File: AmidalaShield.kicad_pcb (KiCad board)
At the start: 4 copper layers, 106 x 73 mm, 32 parts, among them J1 Screw_Terminal_01x02, J2 Micro_SD_Card

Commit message: Switched SD Card slots
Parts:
- removed J2: Micro_SD_Card, Connector_Card:microSD_HC_Wuerth_693072010801
- added J3: Micro_SD_Card, Connector_Card:microSD_HC_Hirose_DM3AT-SF-PEJM5, F.Cu at (146.6, 48.7)
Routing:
- net GND: track 61.9 -> 73.6 mm
- net /SPI/GPIO11: track 133.9 -> 123.2 mm
- net +3.3V: track 106.5 -> 98.7 mm
- net /SPI/GPIO12: track 179.4 -> 171.9 mm
- net /SPI/GPIO13: track 178.9 -> 172.4 mm
- net /SPI/GPIO10: track 86.9 -> 83.8 mm

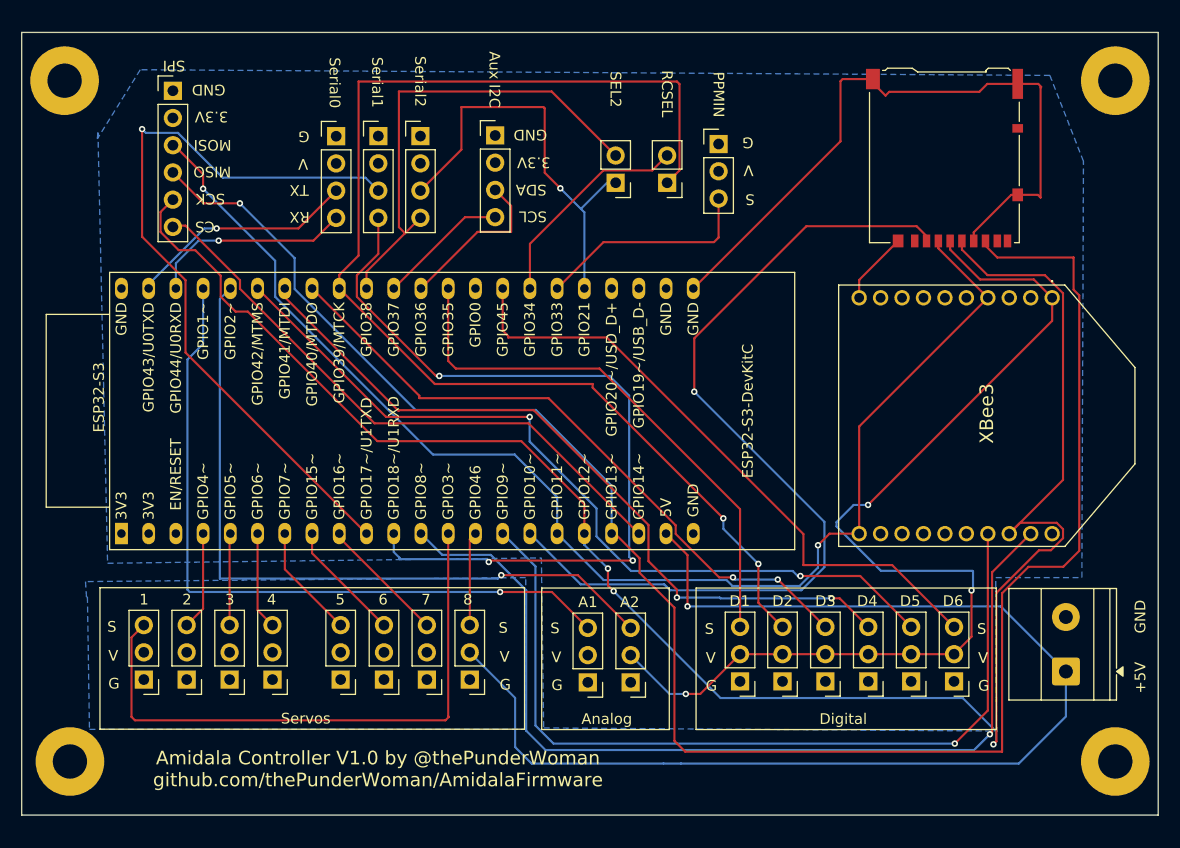
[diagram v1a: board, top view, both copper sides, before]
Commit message: Remapped GPIOs for clean routing
This updates the GPIO table so that the traces and vias are far cleaner. Slight repositioning of some pins to account for that. Rebuilt all gerbers and necessary stuff.
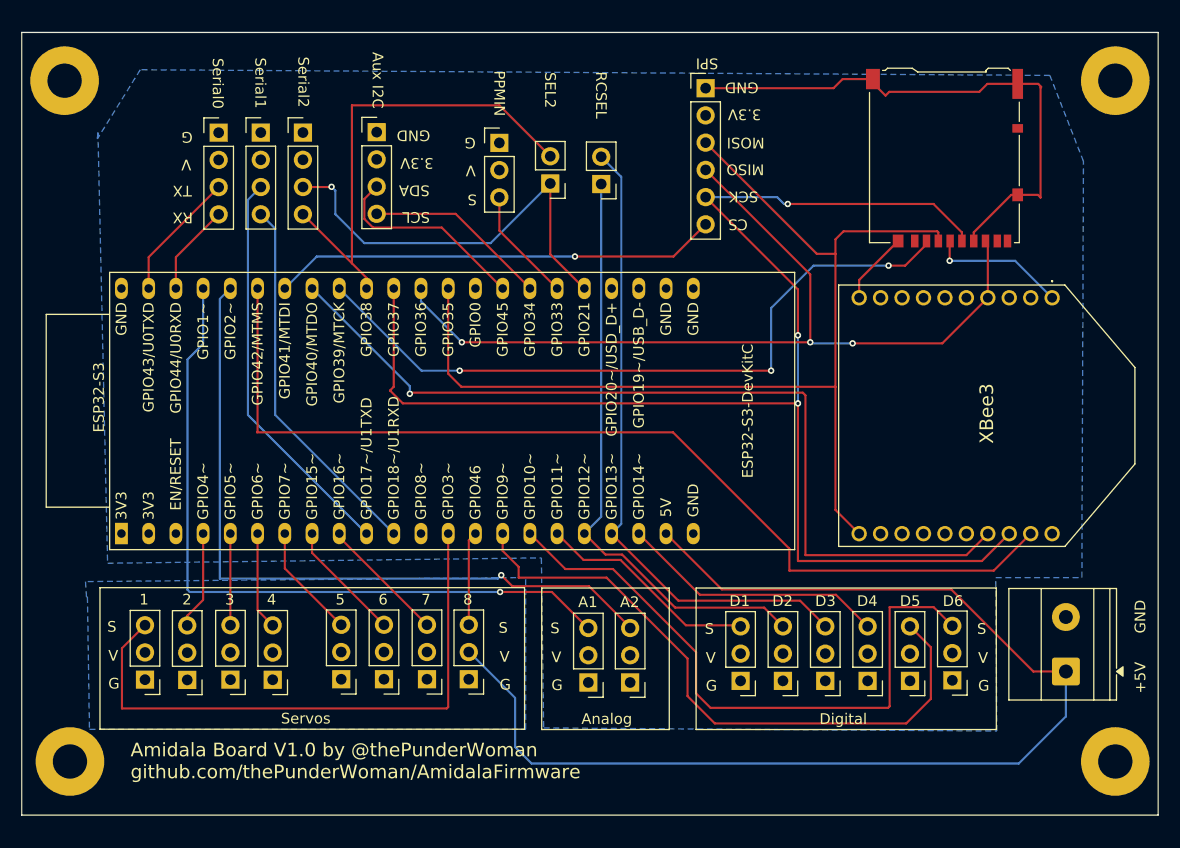
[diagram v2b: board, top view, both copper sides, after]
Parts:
- moved SPI1 49.7 mm to (124.3, 42.2)
- moved J_PPMIN1 20.5 mm to (105.0, 47.3)
- moved I2C1 11.1 mm to (93.6, 46.3)
- moved Serial1 11.0 mm to (82.8, 46.3)
- moved SWSerial1 11.0 mm to (86.7, 46.3)
- moved Serial0 11.0 mm to (78.9, 46.4)
- moved J_RCSEL1 6.15 mm to (114.5, 51.1)
- moved J_SEL2 6.10 mm to (109.8, 51.1)
- moved J_Digital6 0.19 mm to (147.3, 97.4)
- moved J_Digital5 0.12 mm to (143.3, 97.5)
- moved J_Servo1 0.11 mm to (72.0, 97.4)
- moved J_Servo8 0.09 mm to (102.2, 97.3)
- moved J_Servo3 0.08 mm to (80.0, 97.4)
- moved J_Digital4 0.08 mm to (139.4, 97.5)
- moved J_Digital1 0.07 mm to (127.5, 97.5)
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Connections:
- ESP32-S3 pad 12: /SPI/GPIO8 -> unconnected-(ESP32-S3-GPIO8/ADC1_CH7-Pad12)
- ESP32-S3 pad 15: /SPI/GPIO9 -> /Pins/GPIO9
- ESP32-S3 pad 16: /SPI/GPIO10 -> /Pins/GPIO10
- ESP32-S3 pad 17: /SPI/GPIO11 -> /Pins/GPIO11
- ESP32-S3 pad 18: /SPI/GPIO12 -> /Pins/GPIO12
- ESP32-S3 pad 19: /SPI/GPIO13 -> /Pins/GPIO13
- ESP32-S3 pad 20: /SPI/GPIO14 -> /Pins/GPIO14
- ESP32-S3 pad 29: /RC Control/GPIO48 -> /Comms/GPIO48
- ESP32-S3 pad 30: /Pins/GPIO45 -> /Comms/GPIO45
- ESP32-S3 pad 32: /Pins/GPIO35 -> /SPI/GPIO35
- ESP32-S3 pad 33: /Comms/GPIO36 -> /SPI/GPIO36
- ESP32-S3 pad 34: /Comms/GPIO37 -> /SPI/GPIO37
- ESP32-S3 pad 36: /Pins/GPIO39 -> /SPI/GPIO39
- ESP32-S3 pad 37: /Pins/GPIO40 -> /SPI/GPIO40
- ESP32-S3 pad 38: /Pins/GPIO41 -> /SPI/GPIO41
- ESP32-S3 pad 39: /Pins/GPIO42 -> /SPI/GPIO42
- I2C1 pad 3: /Comms/GPIO36 -> /Comms/GPIO45
- I2C1 pad 4: /Comms/GPIO37 -> /Comms/GPIO48
- J3 pad 2: /SPI/GPIO10 -> /SPI/GPIO39
- J3 pad 3: /SPI/GPIO11 -> /SPI/GPIO35
- J3 pad 5: /SPI/GPIO12 -> /SPI/GPIO37
- J3 pad 7: /SPI/GPIO13 -> /SPI/GPIO36
- J_Digital1 pad 3: /Pins/GPIO35 -> /Pins/GPIO11
- J_Digital2 pad 3: /Pins/GPIO39 -> /Pins/GPIO12
- J_Digital3 pad 3: /Pins/GPIO40 -> /Pins/GPIO13
- J_Digital4 pad 3: /Pins/GPIO41 -> /Pins/GPIO14
- J_Digital5 pad 3: /Pins/GPIO42 -> /Pins/GPIO9
- J_Digital6 pad 3: /Pins/GPIO45 -> /Pins/GPIO10
- J_RCSEL1 pad 1: /Pins/GPIO39 -> /Pins/GPIO12
- J_RCSEL1 pad 2: /RC Control/GPIO48 -> /Pins/GPIO13
- SPI1 pad 3: /SPI/GPIO11 -> /SPI/GPIO35
- SPI1 pad 4: /SPI/GPIO13 -> /SPI/GPIO36
- SPI1 pad 5: /SPI/GPIO12 -> /SPI/GPIO37
- SPI1 pad 6: /SPI/GPIO14 -> /SPI/GPIO41
- XBee3 pad 11: /SPI/GPIO11 -> /SPI/GPIO35
- XBee3 pad 17: /SPI/GPIO9 -> /SPI/GPIO40
- XBee3 pad 18: /SPI/GPIO12 -> /SPI/GPIO37
- XBee3 pad 19: /SPI/GPIO8 -> /SPI/GPIO42
- XBee3 pad 4: /SPI/GPIO11 -> /SPI/GPIO36
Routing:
- net /SPI/GPIO13: track 172.4 -> 0.00 mm, vias 1 -> 0
- net /SPI/GPIO12: track 171.9 -> 0.00 mm, vias 3 -> 0
- net /SPI/GPIO37: track 0.00 -> 132.6 mm, vias 0 -> 3
- net /SPI/GPIO11: track 123.2 -> 0.00 mm, vias 2 -> 0
- net /Pins/GPIO39: track 117.1 -> 0.00 mm, vias 2 -> 0
- net /SPI/GPIO35: track 0.00 -> 100.1 mm
- net /SPI/GPIO42: track 0.00 -> 93.6 mm
- net /SPI/GPIO8: track 90.0 -> 0.00 mm, vias 1 -> 0
- net +3.3V: track 98.7 -> 12.9 mm, vias 3 -> 1
- net /SPI/GPIO10: track 83.8 -> 0.00 mm, vias 1 -> 0
- net /SPI/GPIO40: track 0.00 -> 83.4 mm, vias 0 -> 1
- net /SPI/GPIO36: track 0.00 -> 83.0 mm, vias 0 -> 3
- net /SPI/GPIO9: track 79.8 -> 0.00 mm, vias 1 -> 0
- net /Pins/GPIO42: track 76.9 -> 0.00 mm, vias 2 -> 0
- net /Pins/GPIO41: track 70.4 -> 0.00 mm, vias 2 -> 0
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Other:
- board text added: "Amidala Board V1.0 by @thePunderWoman github.com/thePunderWoman/AmidalaFirmware"
- board text removed: "Amidala Controller V1.0 by @thePunderWoman github.com/thePunderWoman/AmidalaFirmware"

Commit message: final pass safety check
This verified that the XBee had all the pins wired up correctly with the proper resistor and cap connections. Glad I caught this before getting them fabbed.
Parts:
- added C1: 100n, Capacitor_SMD:C_0603_1608Metric, F.Cu at (134.1, 60.7)
- added R1: 10k, Resistor_SMD:R_0603_1608Metric, F.Cu at (161.6, 55.2)
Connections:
- ESP32-S3 pad 12: unconnected-(ESP32-S3-GPIO8/ADC1_CH7-Pad12) -> /SPI/GPIO8
- XBee3 pad 13: unconnected-(XBee3-ON/~{SLEEP}/DIO9-Pad13) -> /SPI/GPIO8
- XBee3 pad 5: unconnected-(XBee3-~{RESET}-Pad5) -> Net-(XBee3-~{RESET})
- XBee3 pad 9: unconnected-(XBee3-~{DTR}/SLEEP_RQ/DIO8-Pad9) -> GND
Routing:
- net /SPI/GPIO8: track 0.00 -> 47.7 mm, vias 0 -> 1
- net Net-(XBee3-~{RESET}): track 0.00 -> 32.6 mm, vias 0 -> 2
- net +3.3V: track 12.9 -> 21.8 mm
- net GND: track 61.0 -> 66.5 mm, vias 0 -> 1
- net /SPI/GPIO36: track 83.0 -> 85.3 mm

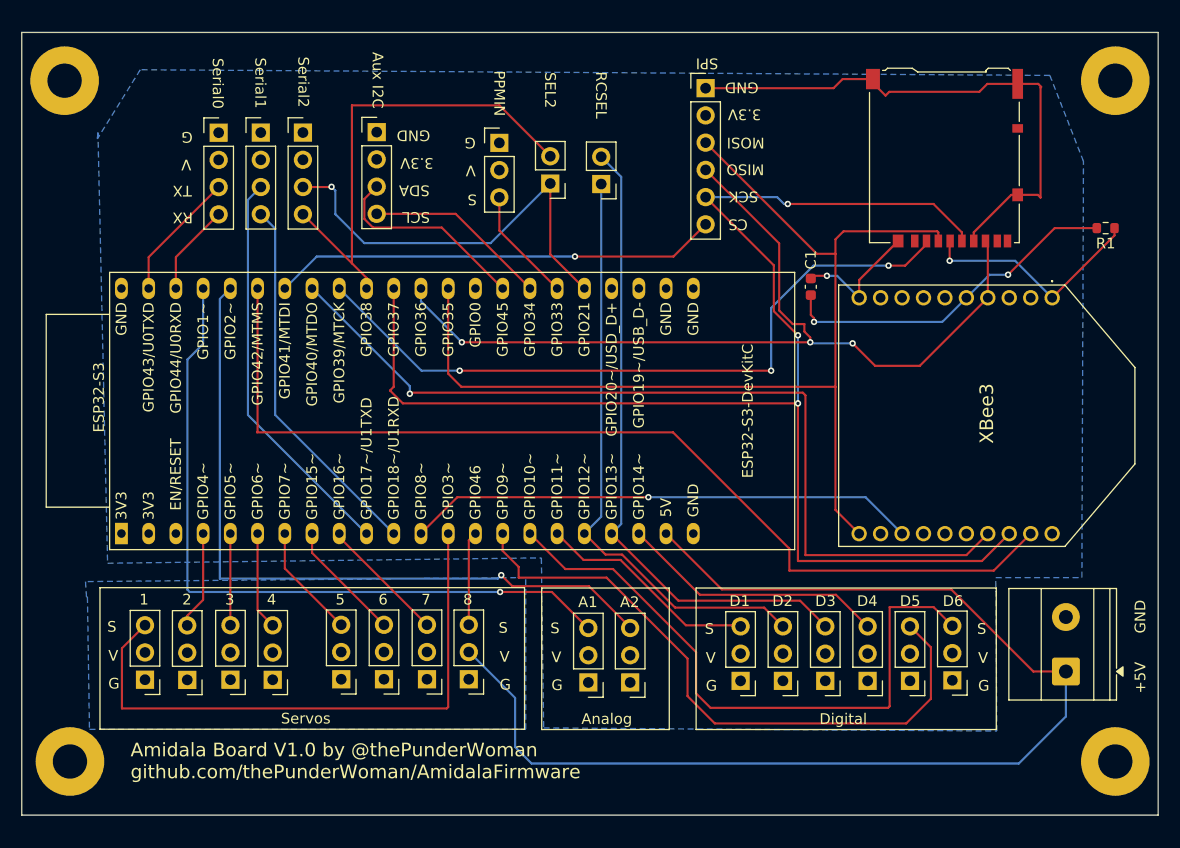
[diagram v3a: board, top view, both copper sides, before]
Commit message: Updated to v1.1 to fix issues
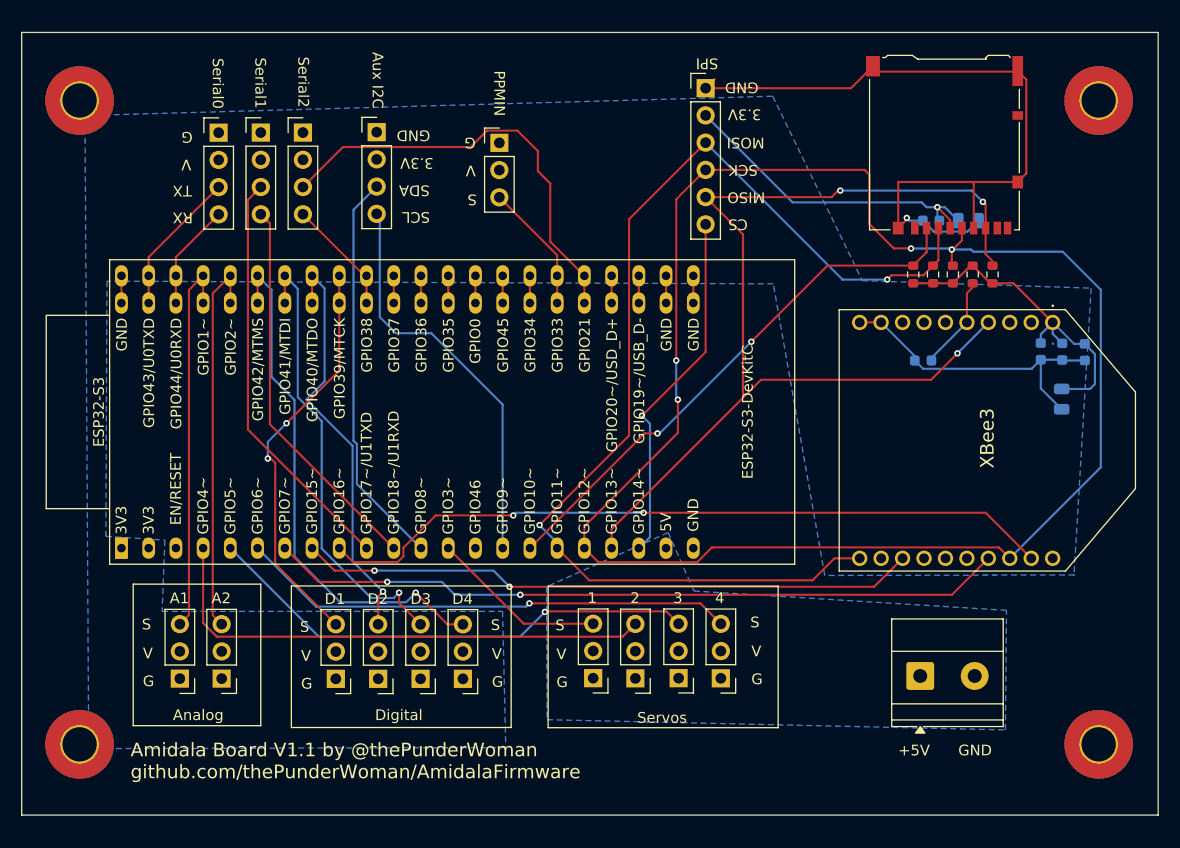
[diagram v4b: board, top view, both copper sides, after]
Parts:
- removed J_Digital5: D5, Connector_PinHeader_2.54mm:PinHeader_1x03_P2.54mm_Vertical
- removed J_Digital6: D6, Connector_PinHeader_2.54mm:PinHeader_1x03_P2.54mm_Vertical
- removed J_RCSEL1: RCSEL, Connector_PinHeader_2.54mm:PinHeader_1x02_P2.54mm_Vertical
- removed J_SEL2: RCSEL2, Connector_PinHeader_2.54mm:PinHeader_1x02_P2.54mm_Vertical
- removed J_Servo5: 5, Connector_PinHeader_2.54mm:PinHeader_1x03_P2.54mm_Vertical
- removed J_Servo6: 6, Connector_PinHeader_2.54mm:PinHeader_1x03_P2.54mm_Vertical
- removed J_Servo7: 7, Connector_PinHeader_2.54mm:PinHeader_1x03_P2.54mm_Vertical
- removed J_Servo8: 8, Connector_PinHeader_2.54mm:PinHeader_1x03_P2.54mm_Vertical
- removed the REF** at (65.0, 105.0)
- removed the REF** at (162.5, 41.5)
- removed the REF** at (64.5, 41.5)
- removed the REF** at (162.5, 105.0)
- added C2: 100n, Capacitor_SMD:C_0603_1608Metric, B.Cu at (155.6, 66.8)
- added C3: 100n, Capacitor_SMD:C_0603_1608Metric, B.Cu at (145.3, 54.5)
- added C4: 10u, Capacitor_SMD:C_0805_2012Metric, B.Cu at (148.8, 54.5)
- added C5: 1u, Capacitor_SMD:C_0603_1608Metric, B.Cu at (159.7, 66.8)
- added C6: 8.2p, Capacitor_SMD:C_0603_1608Metric, B.Cu at (157.6, 66.8)
- added C7: 10u, Capacitor_SMD:C_0805_2012Metric, B.Cu at (157.5, 71.2)
- added G***: LOGO, Amidala:amidala-silkscreen, B.Cu at (113.4, 72.5)
- added R2: 10k, Resistor_SMD:R_0603_1608Metric, F.Cu at (143.7, 59.6)
- added R3: 10k, Resistor_SMD:R_0603_1608Metric, F.Cu at (145.5, 59.6)
- added R4: 10k, Resistor_SMD:R_0603_1608Metric, F.Cu at (147.3, 59.6)
- added R5: 10k, Resistor_SMD:R_0603_1608Metric, F.Cu at (151.1, 59.6)
- added REF**: MountingHole_3.2mm_M3_Pad_TopBottom, MountingHole:MountingHole_3.2mm_M3_Pad_TopBottom, F.Cu at (160.9, 43.4)
- added REF**: MountingHole_3.2mm_M3_Pad_TopBottom, MountingHole:MountingHole_3.2mm_M3_Pad_TopBottom, F.Cu at (65.9, 43.4)
- added REF**: MountingHole_3.2mm_M3_Pad_TopBottom, MountingHole:MountingHole_3.2mm_M3_Pad_TopBottom, F.Cu at (65.9, 103.4)
- added REF**: MountingHole_3.2mm_M3_Pad_TopBottom, MountingHole:MountingHole_3.2mm_M3_Pad_TopBottom, F.Cu at (160.9, 103.4)
- C1: moved to B.Cu
- moved J_Servo1 41.8 mm to (113.8, 97.2)
- moved J_Servo2 41.8 mm to (117.7, 97.2)
- moved J_Servo3 41.8 mm to (121.8, 97.2)
- moved J_Servo4 41.8 mm to (125.7, 97.2)
- moved J_Analog1 38.1 mm to (75.2, 97.3)
- moved J_Analog2 38.1 mm to (79.2, 97.3)
- moved J_Digital1 37.8 mm to (89.8, 97.3)
- moved J_Digital2 37.8 mm to (93.8, 97.3)
- moved J_Digital4 37.8 mm to (101.7, 97.3)
- moved J_Digital3 37.8 mm to (97.7, 97.3)
- moved J1 13.6 mm to (144.3, 97.0), turned to 0 degrees
- moved R1 13.1 mm to (149.2, 59.6), turned to -90 degrees
- moved C1 12.5 mm to (144.6, 67.6), turned to 180 degrees
- moved XBee3 2.30 mm to (156.7, 64.0)
- moved ESP32-S3 1.36 mm to (69.8, 85.1)
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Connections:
- ESP32-S3 pad 12: /SPI/GPIO8 -> /Comms/GPIO8
- ESP32-S3 pad 14: /Servos/GPIO46 -> unconnected-(ESP32-S3-GPIO46-Pad14)
- ESP32-S3 pad 15: /Pins/GPIO9 -> /Comms/GPIO9
- ESP32-S3 pad 16: /Pins/GPIO10 -> /SPI/GPIO10
- ESP32-S3 pad 17: /Pins/GPIO11 -> /SPI/GPIO11
- ESP32-S3 pad 18: /Pins/GPIO12 -> /SPI/GPIO12
- ESP32-S3 pad 19: /Pins/GPIO13 -> /SPI/GPIO13
- ESP32-S3 pad 20: /Pins/GPIO14 -> /SPI/GPIO14
- ESP32-S3 pad 29: /Comms/GPIO48 -> unconnected-(ESP32-S3-GPIO48-Pad29)
- ESP32-S3 pad 30: /Comms/GPIO45 -> unconnected-(ESP32-S3-GPIO45-Pad30)
- ESP32-S3 pad 32: /SPI/GPIO35 -> unconnected-(ESP32-S3-GPIO35-Pad32)
- ESP32-S3 pad 33: /SPI/GPIO36 -> unconnected-(ESP32-S3-GPIO36-Pad33)
- ESP32-S3 pad 34: /SPI/GPIO37 -> unconnected-(ESP32-S3-GPIO37-Pad34)
- ESP32-S3 pad 36: /SPI/GPIO39 -> /Pins/GPIO39
- ESP32-S3 pad 37: /SPI/GPIO40 -> /Pins/GPIO40
- ESP32-S3 pad 38: /SPI/GPIO41 -> /Pins/GPIO41
- ESP32-S3 pad 39: /SPI/GPIO42 -> /Pins/GPIO42
- ESP32-S3 pad 7: /Servos/GPIO7 -> /SPI/GPIO7
- ESP32-S3 pad 8: /Servos/GPIO15 -> /SPI/GPIO15
- ESP32-S3 pad 9: /Servos/GPIO16 -> /SPI/GPIO16
- I2C1 pad 3: /Comms/GPIO45 -> /Comms/GPIO8
- I2C1 pad 4: /Comms/GPIO48 -> /Comms/GPIO9
- J3 pad 2: /SPI/GPIO39 -> /SPI/GPIO10
- J3 pad 3: /SPI/GPIO35 -> /SPI/GPIO11
- J3 pad 5: /SPI/GPIO37 -> /SPI/GPIO12
- J3 pad 7: /SPI/GPIO36 -> /SPI/GPIO13
- J_Digital1 pad 3: /Pins/GPIO11 -> /Pins/GPIO39
- J_Digital2 pad 3: /Pins/GPIO12 -> /Pins/GPIO40
- J_Digital3 pad 3: /Pins/GPIO13 -> /Pins/GPIO41
- J_Digital4 pad 3: /Pins/GPIO14 -> /Pins/GPIO42
- SPI1 pad 3: /SPI/GPIO35 -> /SPI/GPIO11
- SPI1 pad 4: /SPI/GPIO36 -> /SPI/GPIO12
- SPI1 pad 5: /SPI/GPIO37 -> /SPI/GPIO13
- SPI1 pad 6: /SPI/GPIO41 -> /SPI/GPIO14
- XBee3 pad 11: /SPI/GPIO35 -> /SPI/GPIO11
- XBee3 pad 13: /SPI/GPIO8 -> /SPI/GPIO15
- XBee3 pad 17: /SPI/GPIO40 -> /SPI/GPIO7
- XBee3 pad 18: /SPI/GPIO37 -> /SPI/GPIO12
- XBee3 pad 19: /SPI/GPIO42 -> /SPI/GPIO16
- XBee3 pad 4: /SPI/GPIO36 -> /SPI/GPIO13
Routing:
- net /SPI/GPIO12: track 0.00 -> 158.0 mm, vias 0 -> 4
- net /SPI/GPIO37: track 132.6 -> 0.00 mm, vias 3 -> 0
- net +5V: track 111.1 -> 0.00 mm
- net /SPI/GPIO11: track 0.00 -> 106.0 mm, vias 0 -> 2
- net /SPI/GPIO35: track 100.1 -> 0.00 mm
- net /SPI/GPIO13: track 0.00 -> 97.7 mm, vias 0 -> 3
- net /SPI/GPIO42: track 93.6 -> 0.00 mm
- net /SPI/GPIO36: track 85.3 -> 0.00 mm, vias 3 -> 0
- net /SPI/GPIO40: track 83.4 -> 0.00 mm, vias 1 -> 0
- net /SPI/GPIO16: track 0.00 -> 69.2 mm, vias 0 -> 2
- net /SPI/GPIO7: track 0.00 -> 68.8 mm, vias 0 -> 2
- net /SPI/GPIO39: track 66.6 -> 0.00 mm, vias 3 -> 0
- net /Pins/GPIO13: track 59.9 -> 0.00 mm
- net /Pins/GPIO9: track 59.4 -> 0.00 mm
- net /Pins/GPIO10: track 58.4 -> 0.00 mm
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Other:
- board text added: "Amidala Board V1.1 by @thePunderWoman github.com/thePunderWoman/AmidalaFirmware"
- board text removed: "5"
- board text removed: "6"
- board text removed: "7"
- board text removed: "8"
- board text removed: "Amidala Board V1.0 by @thePunderWoman github.com/thePunderWoman/AmidalaFirmware"
- board text removed: "D5"
- board text removed: "D6"
- board text removed: "GPIO0"
- board text removed: "RCSEL"
- board text removed: "SEL2"

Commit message: Updated to v1.2 to address remaining issues
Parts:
- removed R4: 10k, Resistor_SMD:R_0603_1608Metric
- added C9: 100µF, Capacitor_Tantalum_SMD:CP_EIA-3216-18_Kemet-A, F.Cu at (139.4, 97.2)
- C1, C2, C3, C4, C5, C6, C7: moved to F.Cu
- moved REF** 6.00 mm to (71.9, 103.6)
- moved REF** 6.00 mm to (71.9, 43.4)
- moved C3 4.88 mm to (146.8, 59.2), turned to -90 degrees
- moved C4 4.40 mm to (149.0, 59.0), turned to -90 degrees
- moved J_Digital2 3.50 mm to (97.2, 97.2)
- moved J_Digital3 3.50 mm to (101.2, 97.2)
- moved J_Servo4 3.50 mm to (129.2, 97.3)
- moved J_Servo1 3.50 mm to (117.3, 97.3)
- moved J_Servo2 3.50 mm to (121.2, 97.3)
- moved J_Servo3 3.50 mm to (125.3, 97.3)
- moved J_Analog1 3.45 mm to (78.7, 97.2)
- moved J_Digital1 3.45 mm to (93.2, 97.2)
- moved J_Analog2 3.45 mm to (82.6, 97.2)
- moved J_Digital4 3.45 mm to (105.1, 97.2)
- moved G*** 2.86 mm to (116.2, 72.8)
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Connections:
- ESP32-S3 pad 1: unconnected-(ESP32-S3-3V3-Pad1) -> +3.3V
- ESP32-S3 pad 2: unconnected-(ESP32-S3-3V3-Pad1)_1 -> +3.3V
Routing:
- net GND: track 107.7 -> 120.0 mm, vias 1 -> 333
- net /Servos/GPIO4: track 48.3 -> 58.6 mm
- net /Servos/GPIO6: track 46.4 -> 52.8 mm, vias 1 -> 0
- net +5V: track 0.00 -> 5.41 mm
- net /Pins/GPIO40: track 39.4 -> 35.4 mm
- net /Comms/GPIO18: track 36.3 -> 39.8 mm
- net /SPI/GPIO12: track 158.0 -> 154.5 mm
- net /Pins/GPIO1: track 35.9 -> 32.5 mm
- net /Pins/GPIO2: track 36.1 -> 33.0 mm
- net /Pins/GPIO39: track 38.5 -> 41.3 mm
- net unconnected-(ESP32-S3-GPIO48-Pad29): track 2.54 -> 0.00 mm
- net unconnected-(ESP32-S3-GPIO45-Pad30): track 2.54 -> 0.00 mm
- net unconnected-(ESP32-S3-GPIO37-Pad34)_1: track 2.54 -> 0.00 mm
- net unconnected-(ESP32-S3-GPIO36-Pad33): track 2.54 -> 0.00 mm
- net unconnected-(ESP32-S3-GPIO35-Pad32)_1: track 2.54 -> 0.00 mm
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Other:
- board size 106 x 73 mm -> 100 x 75 mm
